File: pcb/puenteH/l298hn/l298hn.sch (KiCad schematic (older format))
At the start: 19 parts, among them K1 CONN_3, K2 CONN_3, P1 CONN_2X2, P2 PWR, P3 CONN_2, P4 CONN_2, U1 L298

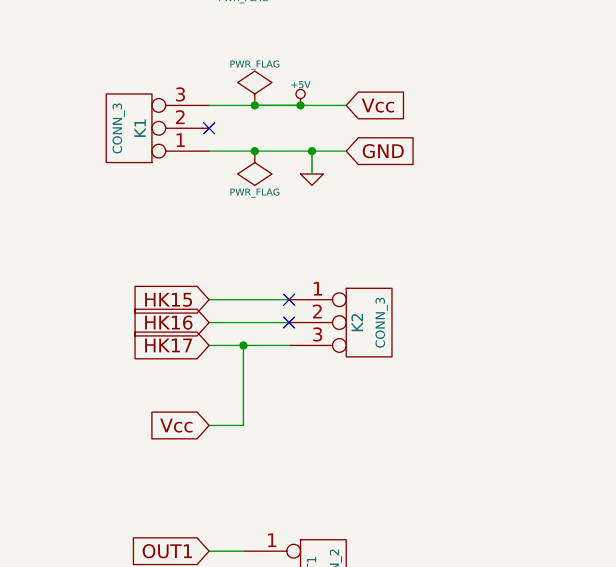
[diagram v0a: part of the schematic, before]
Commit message: Add pull down in shield motors (pins HK15 and HK16) for compatibility with usb4butia v1.8.8
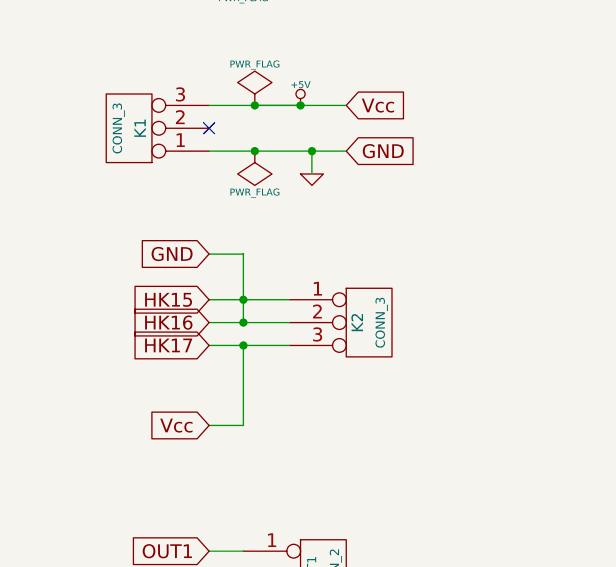
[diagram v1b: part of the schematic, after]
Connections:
- net HK15 is gone; now on net GND: K2.1 (P1)
- net HK16 is gone; now on net GND: K2.2 (PM)
- no-connect marks 5 -> 3
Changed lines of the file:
@@
-EESchema Schematic File Version 2  date lun 29 abr 2013 19:06:31 UYT
+EESchema Schematic File Version 2  date Thu 20 Jun 2013 06:34:06 PM UYT
 LIBS:power
 LIBS:device
@@
 LIBS:contrib
 LIBS:valves
-LIBS:h_bridges
 LIBS:l298hn-cache
-EELAYER 27 0
+EELAYER 24 0
 EELAYER END
 $Descr A4 11693 8268
@@
 Sheet 1 1
 Title "H-Bridge L298HN"
-Date "29 may 2013"
+Date "20 jun 2013"
 Rev "1.0"
 Comp "Butia 2.0"
@@
 F 0 "D8" H 8850 4300 40  0000 C CNN
 F 1 "DIODE" H 8850 4100 40  0000 C CNN
+F 2 "" H 8850 4200 60  0001 C CNN
+F 3 "" H 8850 4200 60  0001 C CNN
 	1    8850 4200
 	0    -1   -1   0
@@
 F 0 "D7" H 8600 4300 40  0000 C CNN
 F 1 "DIODE" H 8600 4100 40  0000 C CNN
+F 2 "" H 8600 4200 60  0001 C CNN
+F 3 "" H 8600 4200 60  0001 C CNN
 	1    8600 4200
 	0    -1   -1   0
@@
 F 0 "D5" H 8600 3000 40  0000 C CNN
 F 1 "DIODE" H 8600 2800 40  0000 C CNN
+F 2 "" H 8600 2900 60  0001 C CNN
+F 3 "" H 8600 2900 60  0001 C CNN
 	1    8600 2900
 	0    -1   -1   0
@@
 F 0 "D6" H 8850 3000 40  0000 C CNN
 F 1 "DIODE" H 8850 2800 40  0000 C CNN
+F 2 "" H 8850 2900 60  0001 C CNN
+F 3 "" H 8850 2900 60  0001 C CNN
 	1    8850 2900
 	0    -1   -1   0
@@
 F 0 "D4" H 8050 4300 40  0000 C CNN
 F 1 "DIODE" H 8050 4100 40  0000 C CNN
+F 2 "" H 8050 4200 60  0001 C CNN
+F 3 "" H 8050 4200 60  0001 C CNN
 	1    8050 4200
 	0    -1   -1   0
@@
 F 0 "D3" H 7800 4300 40  0000 C CNN
 F 1 "DIODE" H 7800 4100 40  0000 C CNN
+F 2 "" H 7800 4200 60  0001 C CNN
+F 3 "" H 7800 4200 60  0001 C CNN
 	1    7800 4200
 	0    -1   -1   0
@@
 F 0 "D1" H 7800 3000 40  0000 C CNN
 F 1 "DIODE" H 7800 2800 40  0000 C CNN
+F 2 "" H 7800 2900 60  0001 C CNN
+F 3 "" H 7800 2900 60  0001 C CNN
 	1    7800 2900
 	0    -1   -1   0
@@
 F 0 "D2" H 8050 3000 40  0000 C CNN
 F 1 "DIODE" H 8050 2800 40  0000 C CNN
+F 2 "" H 8050 2900 60  0001 C CNN
+F 3 "" H 8050 2900 60  0001 C CNN
 	1    8050 2900
 	0    -1   -1   0
@@
 F 0 "P2" V 3900 1550 40  0000 C CNN
 F 1 "PWR" V 4000 1550 40  0000 C CNN
+F 2 "" H 3950 1550 60  0001 C CNN
+F 3 "" H 3950 1550 60  0001 C CNN
 	1    3950 1550
 	1    0    0    -1
@@
 F 0 "MOT2" V 3650 4750 40  0000 C CNN
 F 1 "CONN_2" V 3750 4750 40  0000 C CNN
+F 2 "" H 3700 4750 60  0001 C CNN
+F 3 "" H 3700 4750 60  0001 C CNN
 	1    3700 4750
 	1    0    0    -1
@@
 F 0 "MOT1" V 3650 4350 40  0000 C CNN
 F 1 "CONN_2" V 3750 4350 40  0000 C CNN
+F 2 "" H 3700 4350 60  0001 C CNN
+F 3 "" H 3700 4350 60  0001 C CNN
 	1    3700 4350
 	1    0    0    -1
@@
 F 0 "P1" H 3350 5700 50  0000 C CNN
 F 1 "CONN_2X2" H 3360 5420 40  0000 C CNN
+F 2 "" H 3350 5550 60  0001 C CNN
+F 3 "" H 3350 5550 60  0001 C CNN
 	1    3350 5550
 	1    0    0    -1
@@
 F 0 "K1" V 2800 2400 50  0000 C CNN
 F 1 "CONN_3" V 2900 2400 40  0000 C CNN
+F 2 "" H 2850 2400 60  0001 C CNN
+F 3 "" H 2850 2400 60  0001 C CNN
 	1    2850 2400
 	-1   0    0    1
@@
 F 0 "#PWR01" H 3600 2390 20  0001 C CNN
 F 1 "+5V" H 3600 2390 30  0000 C CNN
+F 2 "" H 3600 2300 60  0001 C CNN
+F 3 "" H 3600 2300 60  0001 C CNN
 	1    3600 2300
 	1    0    0    -1
@@
 F 0 "#PWR02" H 3650 2600 30  0001 C CNN
 F 1 "GND" H 3650 2530 30  0001 C CNN
+F 2 "" H 3650 2600 60  0001 C CNN
+F 3 "" H 3650 2600 60  0001 C CNN
 	1    3650 2600
 	1    0    0    -1
@@
 F 0 "#FLG03" H 3400 2595 30  0001 C CNN
 F 1 "PWR_FLAG" H 3400 2680 30  0000 C CNN
+F 2 "" H 3400 2500 60  0001 C CNN
+F 3 "" H 3400 2500 60  0001 C CNN
 	1    3400 2500
 	-1   0    0    1
@@
 F 0 "#FLG04" H 3400 2395 30  0001 C CNN
 F 1 "PWR_FLAG" H 3400 2480 30  0000 C CNN
+F 2 "" H 3400 2300 60  0001 C CNN
+F 3 "" H 3400 2300 60  0001 C CNN
 	1    3400 2300
 	1    0    0    -1
@@
 F 0 "#FLG05" H 3350 1745 30  0001 C CNN
 F 1 "PWR_FLAG" H 3350 1830 30  0000 C CNN
+F 2 "" H 3350 1650 60  0001 C CNN
+F 3 "" H 3350 1650 60  0001 C CNN
 	1    3350 1650
 	-1   0    0    1
@@
 F 0 "P3" V 3700 6200 40  0000 C CNN
 F 1 "CONN_2" V 3800 6200 40  0000 C CNN
+F 2 "" H 3750 6200 60  0001 C CNN
+F 3 "" H 3750 6200 60  0001 C CNN
 	1    3750 6200
 	1    0    0    -1
@@
 F 0 "P4" V 3700 6650 40  0000 C CNN
 F 1 "CONN_2" V 3800 6650 40  0000 C CNN
+F 2 "" H 3750 6650 60  0001 C CNN
+F 3 "" H 3750 6650 60  0001 C CNN
 	1    3750 6650
 	1    0    0    -1
@@
 F 0 "K2" V 3850 3250 50  0000 C CNN
 F 1 "CONN_3" V 3950 3250 40  0000 C CNN
+F 2 "" H 3900 3250 60  0001 C CNN
+F 3 "" H 3900 3250 60  0001 C CNN
 	1    3900 3250
 	1    0    0    -1
@@
 Wire Wire Line
 	3350 3350 3350 3700
-NoConn ~ 3550 3250
-NoConn ~ 3550 3150
 NoConn ~ 3400 6100
 Text GLabel 3200 4250 0    60   Input ~ 0
@@
 Text GLabel 3200 3700 0    60   Input ~ 0
 Vcc
+Text GLabel 3200 2950 0    60   Input ~ 0
+GND
+Wire Wire Line
+	3200 2950 3350 2950
+Wire Wire Line
+	3350 2950 3350 3250
+Connection ~ 3350 3150
+Connection ~ 3350 3250
 $EndSCHEMATC
